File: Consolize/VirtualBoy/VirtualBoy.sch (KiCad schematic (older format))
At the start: 14 parts, among them J1 Conn_01x12, J2 Conn_01x19, J3 Conn_01x19, J4 Barrel Jack, J5 DB15_Female_HighDensity, P6 Conn_01x13, SW1 SW_SPST_LED, SW2 Mode, SW3 Palette, SW4 Boot, U1 74AHCT125N, U2 74AHCT125N

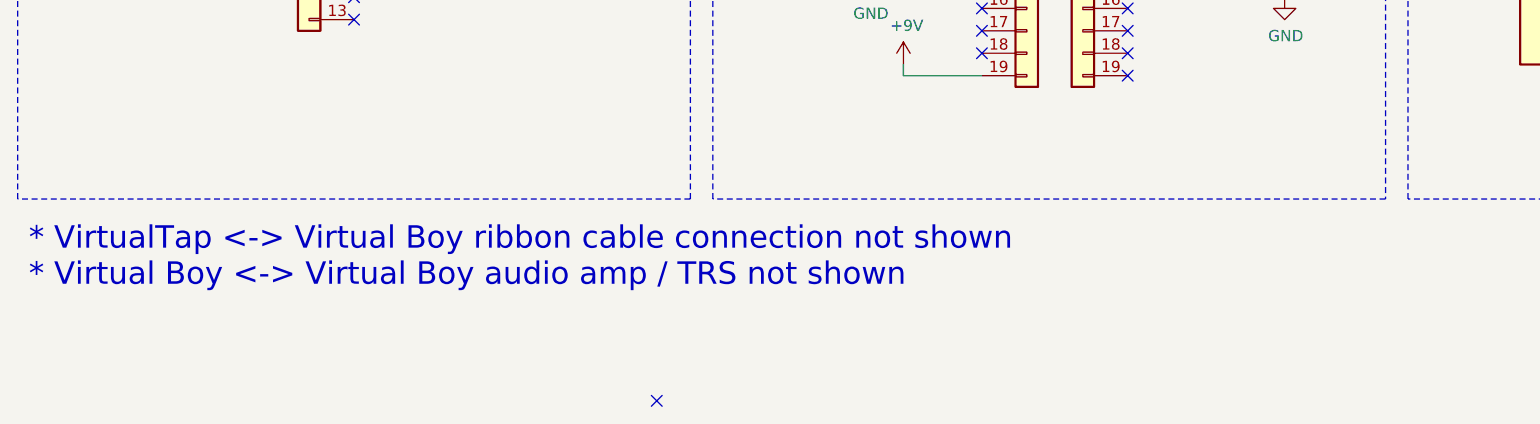
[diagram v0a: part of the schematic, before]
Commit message: Add servo note for VB consolize
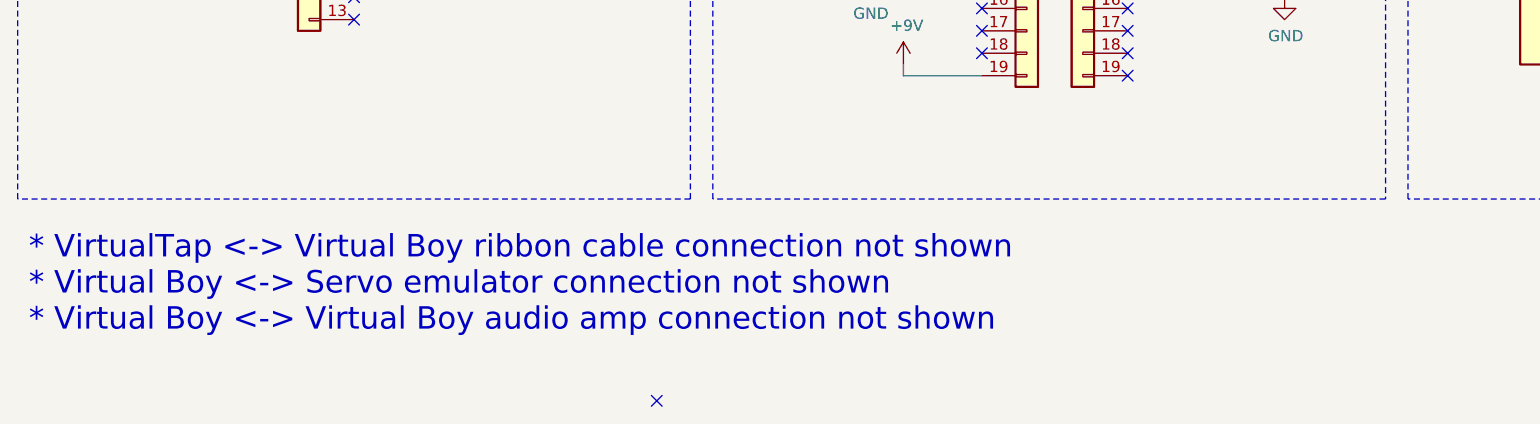
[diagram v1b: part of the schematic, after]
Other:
- note added: "* VirtualTap <-> Virtual Boy ribbon cable connection not shown\n* Virtual Boy <-> Servo emulator connection not shown\n* Virtual Boy <-> Virtual Boy audio amp connection not shown"
- note removed: "* VirtualTap <-> Virtual Boy ribbon cable connection not shown\n* Virtual Boy <-> Virtual Boy audio amp / TRS not shown"
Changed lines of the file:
@@
 NoConn ~ 2800 1900
 NoConn ~ 3750 7300
-Text Notes 950  6800 0    100  ~ 0
-* VirtualTap <-> Virtual Boy ribbon cable connection not shown\n* Virtual Boy <-> Virtual Boy audio amp / TRS not shown
+Text Notes 950  7000 0    100  ~ 0
+* VirtualTap <-> Virtual Boy ribbon cable connection not shown\n* Virtual Boy <-> Servo emulator connection not shown\n* Virtual Boy <-> Virtual Boy audio amp connection not shown
 Wire Wire Line
 	5850 5350 6150 5350
